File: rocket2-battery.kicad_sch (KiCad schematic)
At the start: 83 parts, among them J2 Conn_01x07, J4 SMA, J5 ARM Cortex Debug, P5 PAD_SMD, P6 PAD_SMD, Q2 Q_NMOS_GSD, Q3 Q_NMOS_GSD, Q4 PMOS, Q5 PMOS, Q6 Q_NMOS_GSD, Q7 Q_NMOS_GSD, Q8 PMOS, Q9 PMOS, U5 ADS7828, U6 LM2596S-3.3, U7 LM2596S-5, Y1 16MHz

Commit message: Started layout
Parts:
- C12: footprint (none) -> 0UCIRP-KiCAD-Lib:EEV-FK1V681Q
- C13: footprint (none) -> Capacitor_SMD:CP_Elec_10x12.6
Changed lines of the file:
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@@
 			)
 		)
-		(property "Footprint" ""
+		(property "Footprint" "Capacitor_SMD:CP_Elec_10x12.6"
 			(at 198.12 219.71 0)
 			(effects
@@
 			)
 		)
-		(property "Footprint" ""
+		(property "Footprint" "0UCIRP-KiCAD-Lib:EEV-FK1V681Q"
 			(at 198.12 186.69 0)
 			(effects

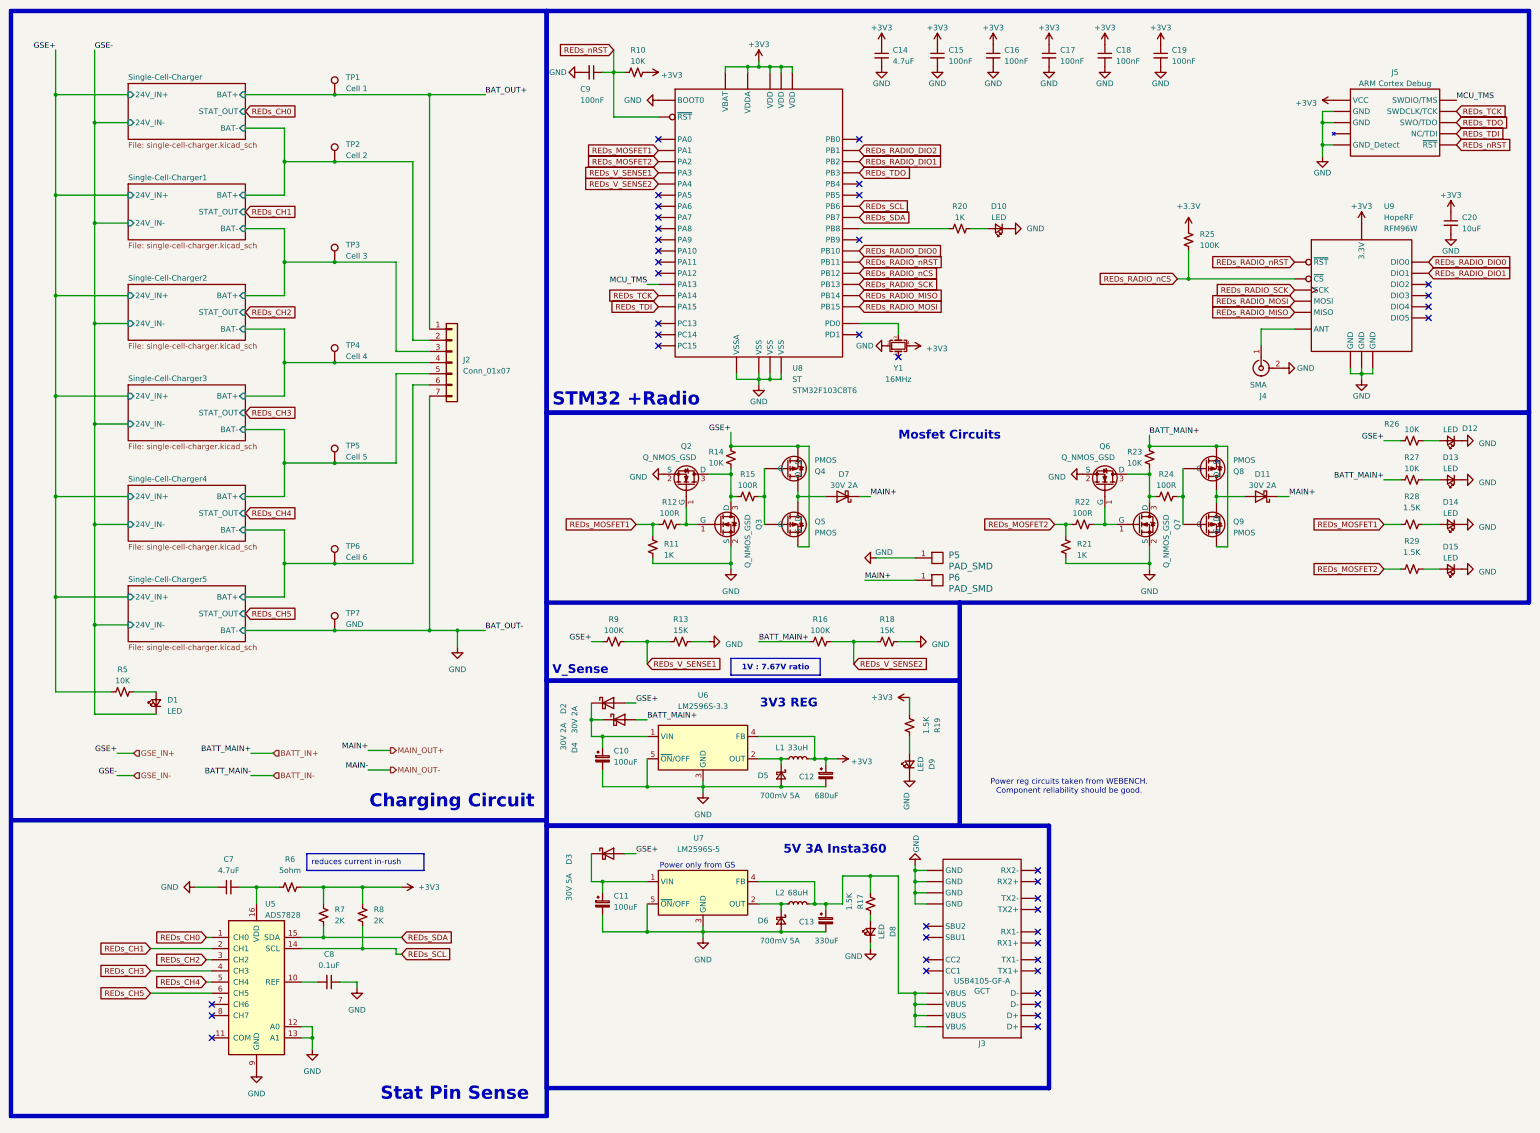
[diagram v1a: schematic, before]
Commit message: Replaced Regs
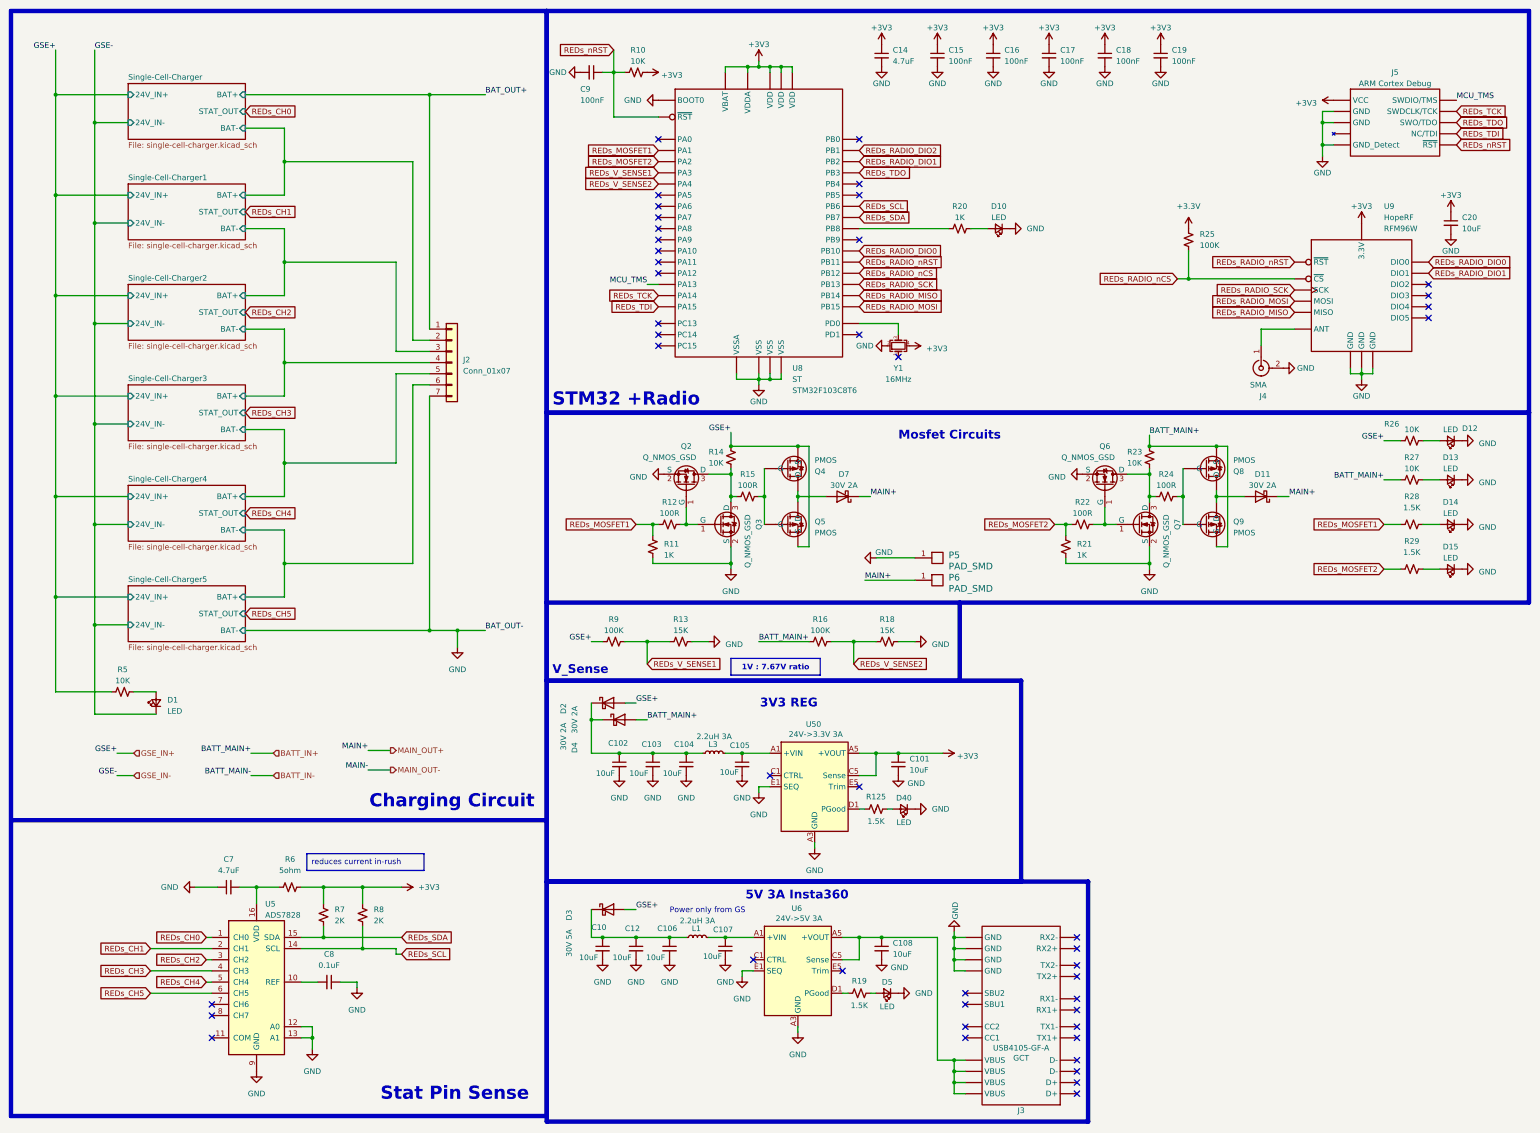
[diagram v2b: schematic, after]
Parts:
- removed C10, C11: 100uF, Capacitor_SMD:CP_Elec_10x10, symbol Device:C_Polarized_Small
- removed C12: 680uF, 0UCIRP-KiCAD-Lib:EEV-FK1V681Q, symbol Device:C_Polarized_Small
- removed C13: 330uF, Capacitor_SMD:CP_Elec_10x12.6, symbol Device:C_Polarized_Small
- removed D5, D6: 700mV 5A, Diode_SMD:D_SMC, symbol Device:D_Schottky_Small
- removed D8, D9: LED, LED_SMD:LED_0603_1608Metric_Pad1.05x0.95mm_HandSolder, symbol Device:LED_Small
- removed L2: 68uH, Inductor_SMD:L_12x12mm_H8mm, symbol Device:L_Small
- removed R17: 1.5K, Resistor_SMD:R_0402_1005Metric, symbol Device:R_Small_US
- removed TP1: Cell 1, TestPoint:TestPoint_Pad_2.0x2.0mm, symbol Connector:TestPoint
- removed TP2: Cell 2, TestPoint:TestPoint_Pad_2.0x2.0mm, symbol Connector:TestPoint
- removed TP3: Cell 3, TestPoint:TestPoint_Pad_2.0x2.0mm, symbol Connector:TestPoint
- removed TP4: Cell 4, TestPoint:TestPoint_Pad_2.0x2.0mm, symbol Connector:TestPoint
- removed TP5: Cell 5, TestPoint:TestPoint_Pad_2.0x2.0mm, symbol Connector:TestPoint
- removed TP6: Cell 6, TestPoint:TestPoint_Pad_2.0x2.0mm, symbol Connector:TestPoint
- removed TP7: GND, TestPoint:TestPoint_Pad_2.0x2.0mm, symbol Connector:TestPoint
- removed U6: LM2596S-3.3, Package_TO_SOT_SMD:TO-263-5_TabPin3, symbol Regulator_Switching:LM2596S-3.3
- removed U7: LM2596S-5, Package_TO_SOT_SMD:TO-263-5_TabPin3, symbol Regulator_Switching:LM2596S-5
- added C10, C102, C103, C104, C105, C106, C107, C12: 10uF, Capacitor_SMD:C_1210_3225Metric, symbol Device:C_Small
- added C101, C108: 10uF, Capacitor_SMD:C_1206_3216Metric, symbol Device:C_Small
- added D40, D5: LED, LED_SMD:LED_0603_1608Metric_Pad1.05x0.95mm_HandSolder, symbol Device:LED_Small
- added L3: 2.2uH 3A, Inductor_SMD:L_Vishay_IHLP-1212, symbol Device:L_Small
- added R125: 1.5K, Resistor_SMD:R_0402_1005Metric, symbol Device:R_Small_US
- added U50: 24V->3.3V 3A, Converter_DCDC:Converter_DCDC_RECOM_RPMx.x-x.0, symbol Converter_DCDC:RPM3.3-6.0
- added U6: 24V->5V 3A, Converter_DCDC:Converter_DCDC_RECOM_RPMx.x-x.0, symbol Converter_DCDC:RPM3.3-6.0
- L1: value 33uH -> 2.2uH 3A; footprint Inductor_SMD:L_12x12mm_H8mm -> Inductor_SMD:L_Vishay_IHLP-1212; Manufacturer Coilcraft -> Vishay Dale; Part # MSS1210-333MEB -> IHLP1212BZER2R2M11
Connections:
- net +3V3: now also C101.1, U50.A5 (+VOUT), U50.B5 (+VOUT), U50.C5 (Sense); no longer L1.2, R19.1
- net GND: now also C10.2, C101.2, C102.2, C103.2, C104.2, C105.2, C106.2, C107.2, C108.2, C12.2, D40.1 (K), D5.1 (K), U50.A3 (GND), U50.A4 (GND), U50.B1 (GND), U50.B2 (GND), U50.B3 (GND), U50.B4 (GND), U50.C2 (GND), U50.C3 (GND), U50.C4 (GND), U50.D2 (GND), U50.D3 (GND), U50.D4 (GND), U50.D5 (GND), U50.E1 (SEQ), U50.E3 (GND), U50.E4 (GND), U6.A3 (GND), U6.A4 (GND), U6.B1 (GND), U6.B2 (GND), U6.B3 (GND), U6.B4 (GND), U6.C2 (GND), U6.C3 (GND), U6.C4 (GND), U6.D2 (GND), U6.D3 (GND), U6.D4 (GND), U6.D5 (GND), U6.E1 (SEQ), U6.E3 (GND), U6.E4 (GND)
- net at J3.A4 (VBUS), J3.A9 (VBUS), J3.B4 (VBUS)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: now also C108.1, U6.A5 (+VOUT), U6.B5 (+VOUT), U6.C5 (Sense)
- net at D3.1 (K): now also L1.1, C10.1, C106.1, C12.1
- net at R19.2: now also D5.2 (A)
- net at D2.1 (K), D4.1 (K): now also C102.1, C103.1, C104.1, L3.1
- new net: C105.1, L3.2, U50.A1 (+VIN), U50.A2 (+VIN)
- new net: C107.1, L1.2, U6.A1 (+VIN), U6.A2 (+VIN)
- new net: R19.1, U6.D1 (PGood)
- new net: R125.1, U50.D1 (PGood)
- new net: D40.2 (A), R125.2
- no-connect marks 41 -> 45
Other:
- note removed: "Power reg circuits taken from WEBENCH. Component reliability should be good."
- moved on the sheet: D3, J3

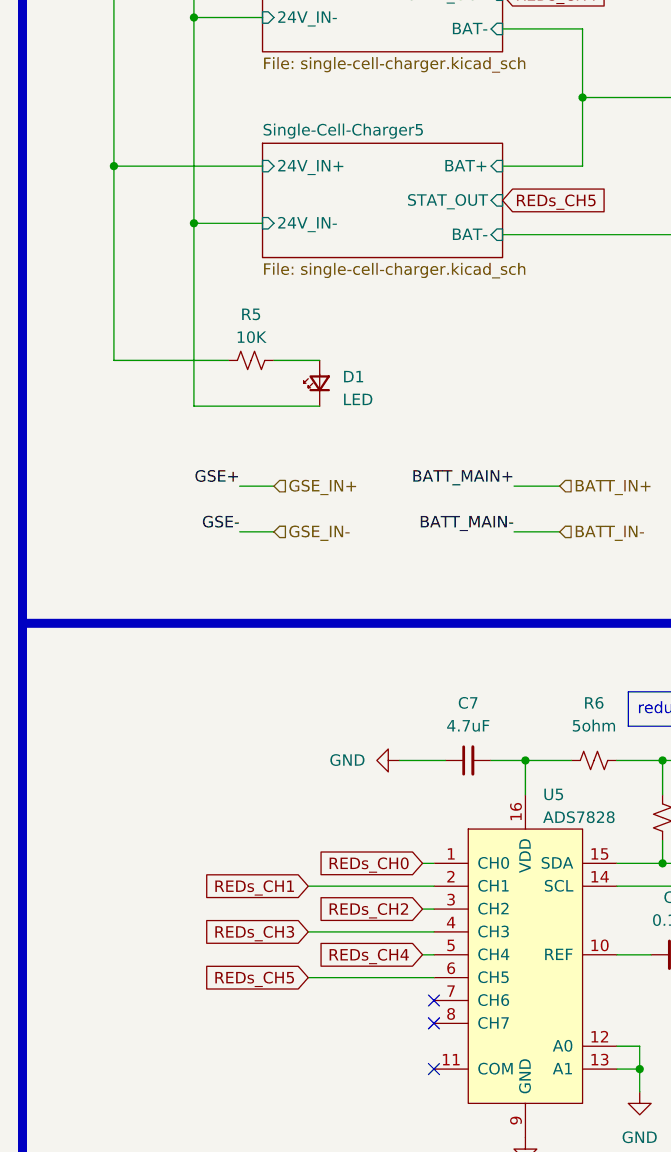
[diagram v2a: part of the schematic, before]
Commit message: All parts on board, starting routing
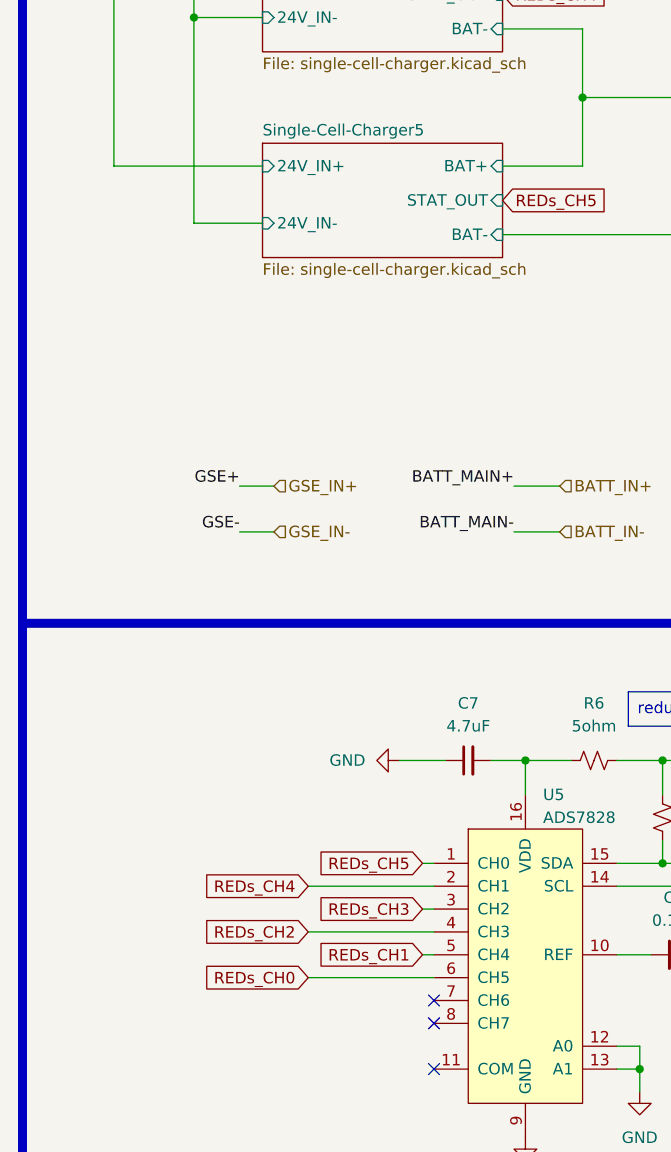
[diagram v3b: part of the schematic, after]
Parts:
- removed D1: LED, LED_SMD:LED_0603_1608Metric_Pad1.05x0.95mm_HandSolder, symbol Device:LED_Small
- removed R5: 10K, Resistor_SMD:R_0402_1005Metric, symbol Device:R_Small_US
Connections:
- net REDs_CH0: now also U5.6 (CH5); no longer U5.1 (CH0)
- net REDs_CH1: now also U5.5 (CH4); no longer U5.2 (CH1)
- net REDs_CH2: now also U5.4 (CH3); no longer U5.3 (CH2)
- net REDs_CH3: now also U5.3 (CH2); no longer U5.4 (CH3)
- net REDs_CH4: now also U5.2 (CH1); no longer U5.5 (CH4)
- net REDs_CH5: now also U5.1 (CH0); no longer U5.6 (CH5)
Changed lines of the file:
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@@
 	)
 	(junction
-		(at 31.75 152.4)
-		(diameter 0)
-		(color 0 0 0 0)
-	)
-	(junction
 		(at 214.63 181.61)
 		(diameter 0)
@@
 	)
 	(junction
-		(at 22.86 146.05)
-		(diameter 0)
-		(color 0 0 0 0)
-	)
-	(junction
 		(at 227.33 251.46)
 		(diameter 0)
@@
 	(wire
 		(pts
-			(xy 22.86 146.05) (xy 22.86 167.64)
-		)
-		(stroke
-			(width 0)
-			(type default)
-		)
-	)
-	(wire
-		(pts
 			(xy 57.15 228.6) (xy 58.42 228.6)
 		)
@@
 	(wire
 		(pts
-			(xy 31.75 152.4) (xy 31.75 172.72)
-		)
-		(stroke
-			(width 0)
-			(type default)
-		)
-	)
-	(wire
-		(pts
 			(xy 147.32 223.52) (xy 154.94 223.52)
 		)
@@
 	(wire
 		(pts
-			(xy 31.75 172.72) (xy 45.72 172.72)
-		)
-		(stroke
-			(width 0)
-			(type default)
-		)
-	)
-	(wire
-		(pts
 			(xy 154.94 129.54) (xy 158.75 129.54)
 		)
@@
 	(wire
 		(pts
-			(xy 40.64 167.64) (xy 45.72 167.64)
-		)
-		(stroke
-			(width 0)
-			(type default)
-		)
-	)
-	(wire
-		(pts
 			(xy 325.12 129.54) (xy 328.93 129.54)
 		)
@@
 	(wire
 		(pts
-			(xy 22.86 167.64) (xy 35.56 167.64)
-		)
-		(stroke
-			(width 0)
-			(type default)
-		)
-	)
-	(wire
-		(pts
 			(xy 149.86 26.67) (xy 149.86 36.83)
 		)
@@
 	(global_label "REDs_CH3"
 		(shape input)
-		(at 44.45 231.14 180)
+		(at 57.15 228.6 180)
 		(fields_autoplaced yes)
 		(effects
@@
 		)
 		(property "Intersheetrefs" "${INTERSHEET_REFS}"
-			(at 31.9701 231.14 0)
+			(at 44.6701 228.6 0)
 			(effects
 				(font
@@
 	(global_label "REDs_CH5"
 		(shape input)
-		(at 44.45 236.22 180)
+		(at 57.15 223.52 180)
 		(fields_autoplaced yes)
 		(effects
@@
 		)
 		(property "Intersheetrefs" "${INTERSHEET_REFS}"
-			(at 31.9701 236.22 0)
+			(at 44.6701 223.52 0)
 			(effects
 				(font
@@
 	(global_label "REDs_CH1"
 		(shape input)
-		(at 44.45 226.06 180)
+		(at 57.15 233.68 180)
 		(fields_autoplaced yes)
 		(effects
@@
 		)
 		(property "Intersheetrefs" "${INTERSHEET_REFS}"
-			(at 31.9701 226.06 0)
+			(at 44.6701 233.68 0)
 			(effects
 				(font
@@
 	(global_label "REDs_CH4"
 		(shape input)
-		(at 57.15 233.68 180)
+		(at 44.45 226.06 180)
 		(fields_autoplaced yes)
 		(effects
@@
 		)
 		(property "Intersheetrefs" "${INTERSHEET_REFS}"
-			(at 44.6701 233.68 0)
+			(at 31.9701 226.06 0)
 			(effects
 				(font
@@
 	(global_label "REDs_CH0"
 		(shape input)
-		(at 57.15 223.52 180)
+		(at 44.45 236.22 180)
 		(fields_autoplaced yes)
 		(effects
@@
 		)
 		(property "Intersheetrefs" "${INTERSHEET_REFS}"
-			(at 44.6701 223.52 0)
+			(at 31.9701 236.22 0)
 			(effects
 				(font
@@
 	(global_label "REDs_CH2"
 		(shape input)
-		(at 57.15 228.6 180)
+		(at 44.45 231.14 180)
 		(fields_autoplaced yes)
 		(effects
@@
 		)
 		(property "Intersheetrefs" "${INTERSHEET_REFS}"
-			(at 44.6701 228.6 0)
+			(at 31.9701 231.14 0)
 			(effects
 				(font
@@
 	)
 	(symbol
-		(lib_id "Device:LED_Small")
-		(at 45.72 170.18 90)
-		(unit 1)
-		(exclude_from_sim no)
-		(in_bom yes)
-		(on_board yes)
-		(dnp no)
-		(fields_autoplaced yes)
-		(property "Reference" "D1"
-			(at 48.26 169.4815 90)
-			(effects
-				(font
-					(size 1.27 1.27)
-				)
-				(justify right)
-			)
-		)
-		(property "Value" "LED"
-			(at 48.26 172.0215 90)
-			(effects
-				(font
-					(size 1.27 1.27)
-				)
-				(justify right)
-			)
-		)
-		(property "Footprint" "LED_SMD:LED_0603_1608Metric_Pad1.05x0.95mm_HandSolder"
-			(at 45.72 170.18 90)
-			(effects
-				(font
-					(size 1.27 1.27)
-				)
-				(hide yes)
-			)
-		)
-		(property "Datasheet" "~"
-			(at 45.72 170.18 90)
-			(effects
-				(font
-					(size 1.27 1.27)
-				)
-				(hide yes)
-			)
-		)
-		(property "Description" ""
-			(at 45.72 170.18 0)
-			(effects
-				(font
-					(size 1.27 1.27)
-				)
-				(hide yes)
-			)
-		)
-		(property "Manufacturer" "Generic"
-			(at 45.72 170.18 0)
-			(effects
-				(font
-					(size 1.27 1.27)
-				)
-				(hide yes)
-			)
-		)
-		(property "Part #" "Generic 0603 Green LED"
-			(at 45.72 170.18 0)
-			(effects
-				(font
-					(size 1.27 1.27)
-				)
-				(hide yes)
-			)
-		)
-		(pin "1"
-		)
-		(pin "2"
-		)
-		(instances
-			(project "rocket2-ecu"
-				(path "/02606b2c-b376-4ffb-9781-f9cea3f70994/c8976b66-9d7c-47d1-8ab5-e6fd9c707361"
-					(reference "D1")
-					(unit 1)
-				)
-			)
-			(project "rocket2-battery"
-				(path "/453543af-7e3c-49a0-a644-4bd49c4f86f8"
-					(reference "D1")
-					(unit 1)
-				)
-			)
-		)
-	)
-	(symbol
 		(lib_id "power:GND")
 		(at 114.3 157.48 0)
@@
 					(unit 1)
 				)
-			)
-		)
-	)
-	(symbol
-		(lib_id "Device:R_Small_US")
-		(at 38.1 167.64 90)
-		(unit 1)
-		(exclude_from_sim no)
-		(in_bom yes)
-		(on_board yes)
-		(dnp no)
-		(fields_autoplaced yes)
-		(property "Reference" "R5"
-			(at 38.1 162.56 90)
-			(effects
-				(font
-					(size 1.27 1.27)
-				)
-			)
-		)
-		(property "Value" "10K"
-			(at 38.1 165.1 90)
-			(effects
-				(font
-					(size 1.27 1.27)
-				)
-			)
-		)
-		(property "Footprint" "Resistor_SMD:R_0402_1005Metric"
-			(at 38.1 167.64 0)
-			(effects
-				(font
-					(size 1.27 1.27)
-				)
-				(hide yes)
-			)
-		)
-		(property "Datasheet" "~"
-			(at 38.1 167.64 0)
-			(effects
-				(font
-					(size 1.27 1.27)
-				)
-				(hide yes)
-			)
-		)
-		(property "Description" ""
-			(at 38.1 167.64 0)
-			(effects
-				(font
-					(size 1.27 1.27)
-				)
-				(hide yes)
-			)
-		)
-		(property "Manufacturer" "Generic"
-			(at 38.1 167.64 0)
-			(effects
-				(font
-					(size 1.27 1.27)
-				)
-				(hide yes)
-			)
-		)
-		(property "Part #" "Generic 10K 1% 0402 Resistor"
-			(at 38.1 167.64 0)
-			(effects
-				(font
-					(size 1.27 1.27)
-				)
-				(hide yes)
-			)
-		)
-		(pin "1"
-		)
-		(pin "2"
-		)
-		(instances
-			(project "rocket2-ecu"
-				(path "/02606b2c-b376-4ffb-9781-f9cea3f70994/c8976b66-9d7c-47d1-8ab5-e6fd9c707361"
-					(reference "R5")
-					(unit 1)
-				)
-			)
-			(project "rocket2-battery"
-				(path "/453543af-7e3c-49a0-a644-4bd49c4f86f8"
-					(reference "R1")
-					(unit 1)
-				)

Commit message: Lots of routing
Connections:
- net +3.3V is gone; now on net +3V3: R25.1
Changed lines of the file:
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@@
 	)
 	(symbol
+		(lib_id "power:+3V3")
+		(at 280.67 62.23 0)
+		(unit 1)
+		(exclude_from_sim no)
+		(in_bom yes)
+		(on_board yes)
+		(dnp no)
+		(fields_autoplaced yes)
+		(property "Reference" "#PWR0360"
+			(at 280.67 66.04 0)
+			(effects
+				(font
+					(size 1.27 1.27)
+				)
+				(hide yes)
+			)
+		)
+		(property "Value" "+3V3"
+			(at 280.67 58.42 0)
+			(effects
+				(font
+					(size 1.27 1.27)
+				)
+			)
+		)
+		(property "Footprint" ""
+			(at 280.67 62.23 0)
+			(effects
+				(font
+					(size 1.27 1.27)
+				)
+				(hide yes)
+			)
+		)
+		(property "Datasheet" ""
+			(at 280.67 62.23 0)
+			(effects
+				(font
+					(size 1.27 1.27)
+				)
+				(hide yes)
+			)
+		)
+		(property "Description" ""
+			(at 280.67 62.23 0)
+			(effects
+				(font
+					(size 1.27 1.27)
+				)
+				(hide yes)
+			)
+		)
+		(pin "1"
+		)
+		(instances
+			(project "rocket2-ecu"
+				(path "/02606b2c-b376-4ffb-9781-f9cea3f70994/c8976b66-9d7c-47d1-8ab5-e6fd9c707361"
+					(reference "#PWR0360")
+					(unit 1)
+				)
+			)
+		)
+	)
+	(symbol
 		(lib_name "GND_6")
 		(lib_id "power:GND")
@@
 					(unit 1)
 				)
-			)
-		)
-	)
-	(symbol
-		(lib_id "power:+3.3V")
-		(at 280.67 62.23 0)
-		(unit 1)
-		(exclude_from_sim no)
-		(in_bom yes)
-		(on_board yes)
-		(dnp no)
-		(property "Reference" "#PWR075"
-			(at 280.67 66.04 0)
-			(effects
-				(font
-					(size 1.27 1.27)
-				)
-				(hide yes)
-			)
-		)
-		(property "Value" "+3.3V"
-			(at 280.67 57.15 0)
-			(effects
-				(font
-					(size 1.27 1.27)
-				)
-			)
-		)
-		(property "Footprint" ""
-			(at 280.67 62.23 0)
-			(effects
-				(font
-					(size 1.27 1.27)
-				)
-				(hide yes)
-			)
-		)
-		(property "Datasheet" ""
-			(at 280.67 62.23 0)
-			(effects
-				(font
-					(size 1.27 1.27)
-				)
-				(hide yes)
-			)
-		)
-		(property "Description" "Power symbol creates a global label with name \"+3.3V\""
-			(at 280.67 62.23 0)
-			(effects
-				(font
-					(size 1.27 1.27)
-				)
-				(hide yes)
-			)
-		)
-		(pin "1"
-		)
-		(instances
-			(project "rocket2-ecu"
-				(path "/02606b2c-b376-4ffb-9781-f9cea3f70994/c8976b66-9d7c-47d1-8ab5-e6fd9c707361"
-					(reference "#PWR075")
-					(unit 1)
-				)
